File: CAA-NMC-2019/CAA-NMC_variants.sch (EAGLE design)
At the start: 28 parts, among them IC1 ATTINY85-20SU, J1 M20-9980346

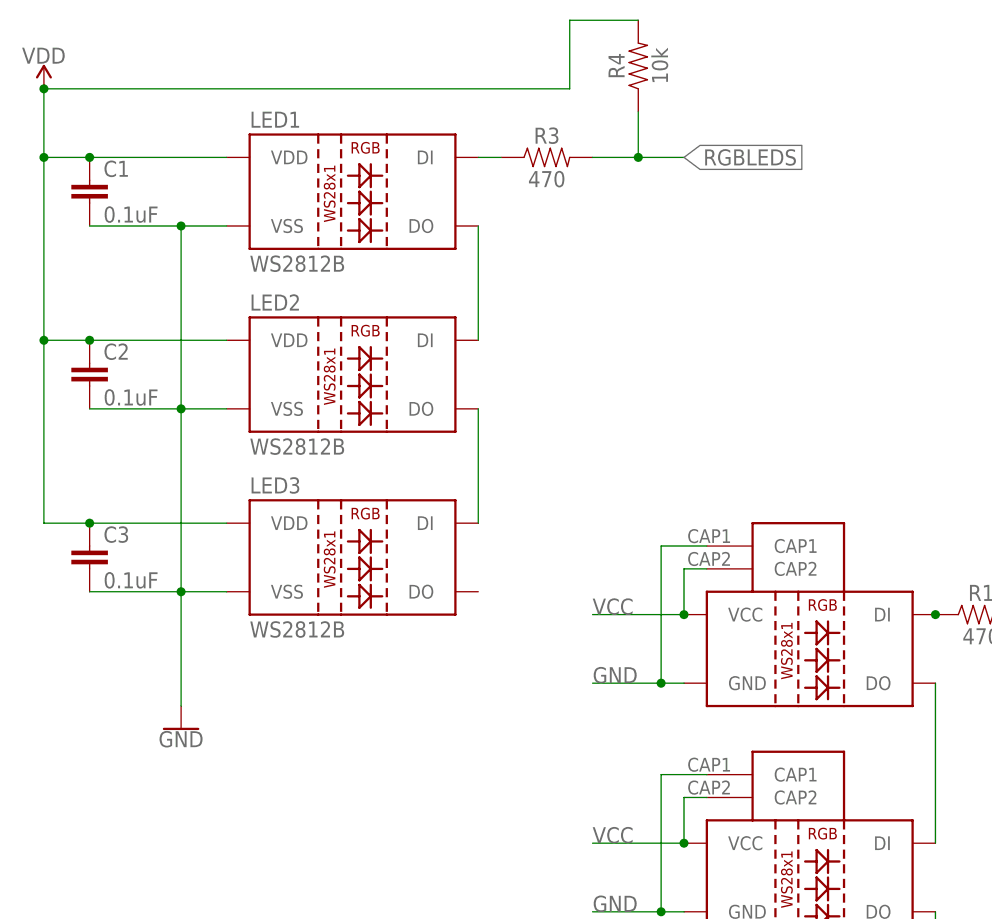
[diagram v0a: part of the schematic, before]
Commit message: added organic layout
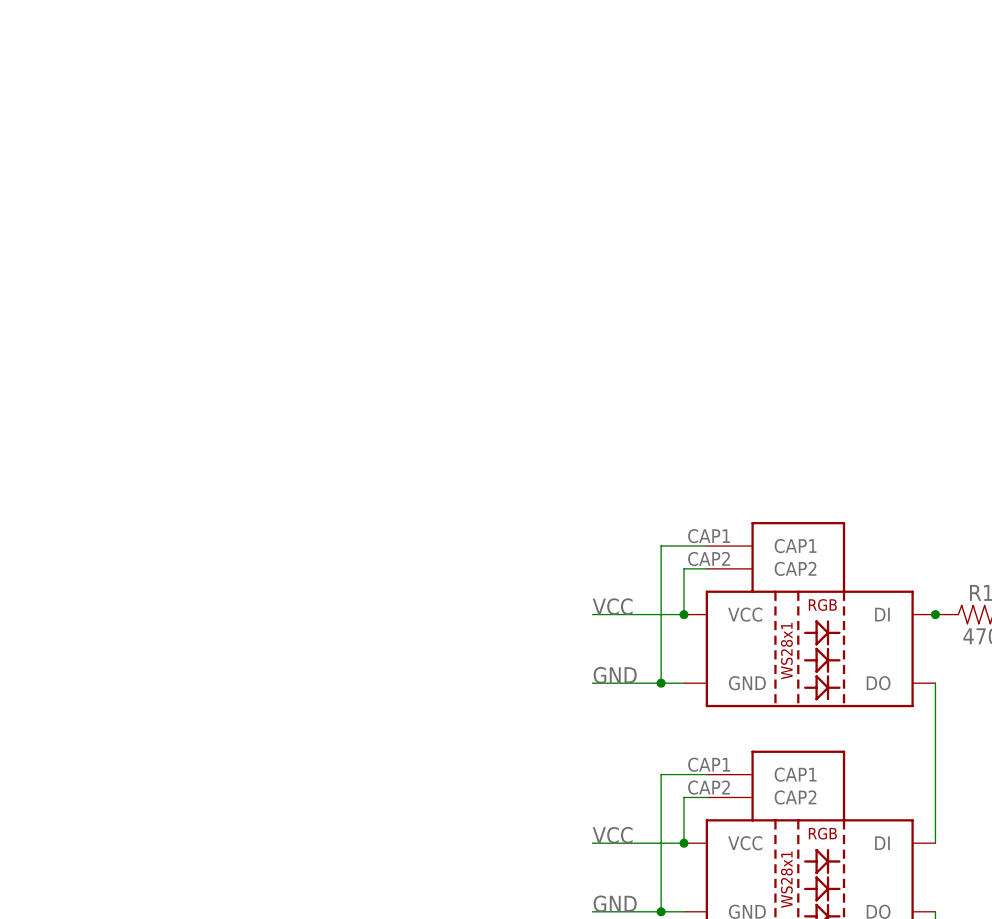
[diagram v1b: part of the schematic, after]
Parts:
- removed C1, C2, C3: 0.1uF, SparkFun-Capacitors:0.1UF-0603-25V-5%
- removed LED1, LED2, LED3: WS2812B, SparkFun-LED:WS2812B
- removed R3: 470, SparkFun-Resistors:470OHM-0603-1/10W-1%
- removed R4: 10k, SparkFun-Resistors:10KOHM-0603-1/10W-1%
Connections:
- removed net N$10: LED2.DO, LED3.DI
- removed net N$12: LED1.DI, R3.1
- removed net N$9: LED1.DO, LED2.DI
- removed net RGBLEDS: R3.2, R4.1
- removed net VDD: C1.1, C2.1, C3.1, LED1.VDD, LED2.VDD, LED3.VDD, R4.2
- net GND: no longer C1.2, C2.2, C3.2, LED1.VSS, LED2.VSS, LED3.VSS
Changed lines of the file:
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@@
 <part name="U$145" library="BadgeParts" deviceset="SMT-SWITCH" device=""/>
 <part name="U$1" library="BadgeParts" deviceset="PROTO" device=""/>
-<part name="LED1" library="SparkFun-LED" library_urn="urn:adsk.eagle:library:529" deviceset="WS2812B" device="" package3d_urn="urn:adsk.eagle:package:39369/1" value="WS2812B"/>
-<part name="SUPPLY5" library="SparkFun-PowerSymbols" library_urn="urn:adsk.eagle:library:530" deviceset="VDD" device=""/>
-<part name="LED2" library="SparkFun-LED" library_urn="urn:adsk.eagle:library:529" deviceset="WS2812B" device="" package3d_urn="urn:adsk.eagle:package:39369/1" value="WS2812B"/>
-<part name="LED3" library="SparkFun-LED" library_urn="urn:adsk.eagle:library:529" deviceset="WS2812B" device="" package3d_urn="urn:adsk.eagle:package:39369/1" value="WS2812B"/>
-<part name="C1" library="SparkFun-Capacitors" library_urn="urn:adsk.eagle:library:510" deviceset="0.1UF" device="-0603-25V-5%" package3d_urn="urn:adsk.eagle:package:37414/1" value="0.1uF"/>
-<part name="C2" library="SparkFun-Capacitors" library_urn="urn:adsk.eagle:library:510" deviceset="0.1UF" device="-0603-25V-5%" package3d_urn="urn:adsk.eagle:package:37414/1" value="0.1uF"/>
-<part name="C3" library="SparkFun-Capacitors" library_urn="urn:adsk.eagle:library:510" deviceset="0.1UF" device="-0603-25V-5%" package3d_urn="urn:adsk.eagle:package:37414/1" value="0.1uF"/>
-<part name="R3" library="SparkFun-Resistors" library_urn="urn:adsk.eagle:library:532" deviceset="470OHM" device="-0603-1/10W-1%" package3d_urn="urn:adsk.eagle:package:39650/1" value="470"/>
-<part name="R4" library="SparkFun-Resistors" library_urn="urn:adsk.eagle:library:532" deviceset="10KOHM" device="-0603-1/10W-1%" package3d_urn="urn:adsk.eagle:package:39650/1" value="10k"/>
-<part name="GND5" library="SparkFun-PowerSymbols" library_urn="urn:adsk.eagle:library:530" deviceset="GND" device=""/>
 <part name="D1" library="BadgeParts" deviceset="WS2812B" device="" package3d_urn="urn:adsk.eagle:package:39369/1" value="WS2812B"/>
 <part name="D2" library="BadgeParts" deviceset="WS2812B" device="" package3d_urn="urn:adsk.eagle:package:39369/1" value="WS2812B"/>
@@
 <instance part="U$145" gate="G$1" x="-180.34" y="129.54" smashed="yes"/>
 <instance part="U$1" gate="G$1" x="-63.5" y="101.6" smashed="yes"/>
-<instance part="LED1" gate="G$1" x="-284.48" y="116.84" smashed="yes">
-<attribute name="NAME" x="-297.18" y="125.222" size="1.778" layer="95"/>
-<attribute name="VALUE" x="-297.18" y="109.22" size="1.778" layer="95"/>
-</instance>
-<instance part="SUPPLY5" gate="VDD" x="-320.04" y="129.54" smashed="yes">
-<attribute name="VALUE" x="-320.04" y="132.334" size="1.778" layer="96" align="bottom-center"/>
-</instance>
-<instance part="LED2" gate="G$1" x="-284.48" y="96.52" smashed="yes">
-<attribute name="NAME" x="-297.18" y="104.902" size="1.778" layer="95"/>
-<attribute name="VALUE" x="-297.18" y="88.9" size="1.778" layer="95"/>
-</instance>
-<instance part="LED3" gate="G$1" x="-284.48" y="76.2" smashed="yes">
-<attribute name="NAME" x="-297.18" y="84.582" size="1.778" layer="95"/>
-<attribute name="VALUE" x="-297.18" y="68.58" size="1.778" layer="95"/>
-</instance>
-<instance part="C1" gate="G$1" x="-314.96" y="116.84" smashed="yes">
-<attribute name="NAME" x="-313.436" y="119.761" size="1.778" layer="95" font="vector"/>
-<attribute name="VALUE" x="-313.436" y="114.681" size="1.778" layer="96" font="vector"/>
-</instance>
-<instance part="C2" gate="G$1" x="-314.96" y="96.52" smashed="yes">
-<attribute name="NAME" x="-313.436" y="99.441" size="1.778" layer="95" font="vector"/>
-<attribute name="VALUE" x="-313.436" y="94.361" size="1.778" layer="96" font="vector"/>
-</instance>
-<instance part="C3" gate="G$1" x="-314.96" y="76.2" smashed="yes">
-<attribute name="NAME" x="-313.436" y="79.121" size="1.778" layer="95" font="vector"/>
-<attribute name="VALUE" x="-313.436" y="74.041" size="1.778" layer="96" font="vector"/>
-</instance>
-<instance part="R3" gate="G$1" x="-264.16" y="121.92" smashed="yes">
-<attribute name="NAME" x="-264.16" y="123.444" size="1.778" layer="95" font="vector" align="bottom-center"/>
-<attribute name="VALUE" x="-264.16" y="120.396" size="1.778" layer="96" font="vector" align="top-center"/>
-</instance>
-<instance part="R4" gate="G$1" x="-254" y="132.08" smashed="yes" rot="R90">
-<attribute name="NAME" x="-255.524" y="132.08" size="1.778" layer="95" font="vector" rot="R90" align="bottom-center"/>
-<attribute name="VALUE" x="-252.476" y="132.08" size="1.778" layer="96" font="vector" rot="R90" align="top-center"/>
-</instance>
-<instance part="GND5" gate="1" x="-304.8" y="58.42" smashed="yes">
-<attribute name="VALUE" x="-304.8" y="58.166" size="1.778" layer="96" align="top-center"/>
-</instance>
 <instance part="D1" gate="G$1" x="-233.68" y="66.04" smashed="yes"/>
 <instance part="D2" gate="G$1" x="-233.68" y="40.64" smashed="yes"/>
@@
 </segment>
 <segment>
-<pinref part="LED3" gate="G$1" pin="VSS"/>
-<pinref part="C3" gate="G$1" pin="2"/>
-<wire x1="-299.72" y1="73.66" x2="-304.8" y2="73.66" width="0.1524" layer="91"/>
-<wire x1="-304.8" y1="73.66" x2="-314.96" y2="73.66" width="0.1524" layer="91"/>
-<junction x="-304.8" y="73.66"/>
-<pinref part="LED2" gate="G$1" pin="VSS"/>
-<pinref part="C2" gate="G$1" pin="2"/>
-<wire x1="-299.72" y1="93.98" x2="-304.8" y2="93.98" width="0.1524" layer="91"/>
-<wire x1="-304.8" y1="93.98" x2="-314.96" y2="93.98" width="0.1524" layer="91"/>
-<wire x1="-304.8" y1="73.66" x2="-304.8" y2="93.98" width="0.1524" layer="91"/>
-<junction x="-304.8" y="93.98"/>
-<pinref part="LED1" gate="G$1" pin="VSS"/>
-<pinref part="C1" gate="G$1" pin="2"/>
-<wire x1="-299.72" y1="114.3" x2="-304.8" y2="114.3" width="0.1524" layer="91"/>
-<wire x1="-304.8" y1="114.3" x2="-314.96" y2="114.3" width="0.1524" layer="91"/>
-<wire x1="-304.8" y1="93.98" x2="-304.8" y2="114.3" width="0.1524" layer="91"/>
-<junction x="-304.8" y="114.3"/>
-<pinref part="GND5" gate="1" pin="GND"/>
-<wire x1="-304.8" y1="73.66" x2="-304.8" y2="60.96" width="0.1524" layer="91"/>
-</segment>
-<segment>
 <pinref part="D1" gate="G$1" pin="GND"/>
 <wire x1="-248.92" y1="63.5" x2="-251.46" y2="63.5" width="0.1524" layer="91"/>
@@
 </segment>
 </net>
-<net name="VDD" class="1">
-<segment>
-<pinref part="LED1" gate="G$1" pin="VDD"/>
-<pinref part="C1" gate="G$1" pin="1"/>
-<wire x1="-299.72" y1="121.92" x2="-314.96" y2="121.92" width="0.1524" layer="91"/>
-<pinref part="SUPPLY5" gate="VDD" pin="VDD"/>
-<wire x1="-314.96" y1="121.92" x2="-320.04" y2="121.92" width="0.1524" layer="91"/>
-<wire x1="-320.04" y1="121.92" x2="-320.04" y2="129.54" width="0.1524" layer="91"/>
-<junction x="-314.96" y="121.92"/>
-<pinref part="LED2" gate="G$1" pin="VDD"/>
-<pinref part="C2" gate="G$1" pin="1"/>
-<wire x1="-299.72" y1="101.6" x2="-314.96" y2="101.6" width="0.1524" layer="91"/>
-<wire x1="-314.96" y1="101.6" x2="-320.04" y2="101.6" width="0.1524" layer="91"/>
-<wire x1="-320.04" y1="101.6" x2="-320.04" y2="121.92" width="0.1524" layer="91"/>
-<junction x="-314.96" y="101.6"/>
-<junction x="-320.04" y="121.92"/>
-<pinref part="LED3" gate="G$1" pin="VDD"/>
-<pinref part="C3" gate="G$1" pin="1"/>
-<wire x1="-299.72" y1="81.28" x2="-314.96" y2="81.28" width="0.1524" layer="91"/>
-<wire x1="-314.96" y1="81.28" x2="-320.04" y2="81.28" width="0.1524" layer="91"/>
-<wire x1="-320.04" y1="81.28" x2="-320.04" y2="101.6" width="0.1524" layer="91"/>
-<junction x="-314.96" y="81.28"/>
-<junction x="-320.04" y="101.6"/>
-<wire x1="-320.04" y1="129.54" x2="-261.62" y2="129.54" width="0.1524" layer="91"/>
-<junction x="-320.04" y="129.54"/>
-<wire x1="-261.62" y1="129.54" x2="-261.62" y2="137.16" width="0.1524" layer="91"/>
-<pinref part="R4" gate="G$1" pin="2"/>
-<wire x1="-261.62" y1="137.16" x2="-254" y2="137.16" width="0.1524" layer="91"/>
-</segment>
-</net>
-<net name="RGBLEDS" class="0">
-<segment>
-<pinref part="R3" gate="G$1" pin="2"/>
-<wire x1="-259.08" y1="121.92" x2="-254" y2="121.92" width="0.1524" layer="91"/>
-<pinref part="R4" gate="G$1" pin="1"/>
-<wire x1="-254" y1="127" x2="-254" y2="121.92" width="0.1524" layer="91"/>
-<wire x1="-254" y1="121.92" x2="-248.92" y2="121.92" width="0.1524" layer="91"/>
-<junction x="-254" y="121.92"/>
-<label x="-248.92" y="121.92" size="1.778" layer="95" xref="yes"/>
-</segment>
-</net>
-<net name="N$9" class="0">
-<segment>
-<pinref part="LED1" gate="G$1" pin="DO"/>
-<pinref part="LED2" gate="G$1" pin="DI"/>
-<wire x1="-271.78" y1="114.3" x2="-271.78" y2="101.6" width="0.1524" layer="91"/>
-</segment>
-</net>
-<net name="N$10" class="0">
-<segment>
-<pinref part="LED2" gate="G$1" pin="DO"/>
-<pinref part="LED3" gate="G$1" pin="DI"/>
-<wire x1="-271.78" y1="93.98" x2="-271.78" y2="81.28" width="0.1524" layer="91"/>
-</segment>
-</net>
-<net name="N$12" class="0">
-<segment>
-<pinref part="LED1" gate="G$1" pin="DI"/>
-<wire x1="-271.78" y1="121.92" x2="-269.24" y2="121.92" width="0.1524" layer="91"/>
-<pinref part="R3" gate="G$1" pin="1"/>
-</segment>
-</net>
